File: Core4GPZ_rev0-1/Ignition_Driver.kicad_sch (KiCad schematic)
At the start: 10 parts, among them Q1 FGP3440G2-F085, Q2 FGP3440G2-F085

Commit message: Reworked the VR conditionner
Schematic and PCB based on the Dropbear model
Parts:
- renumbered D1 to D5, D2 to D6, R1 to R3, R3 to R5
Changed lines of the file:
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@@
 		(dnp no)
 		(fields_autoplaced yes)
-		(property "Reference" "R1"
+		(property "Reference" "R3"
 			(at 76.2 54.61 90)
 			(effects
@@
 			(project "Core4GPZ_rev0-1"
 				(path "/ac28f42d-34b3-4fcc-84dd-ab6106f99610/d5427090-fd08-4b35-ae6e-bc2a7b0d4087"
-					(reference "R1")
+					(reference "R3")
 					(unit 1)
 				)
@@
 		(dnp no)
 		(fields_autoplaced yes)
-		(property "Reference" "#PWR010"
+		(property "Reference" "#PWR08"
 			(at 90.17 85.09 0)
 			(effects
@@
 			(project "Core4GPZ_rev0-1"
 				(path "/ac28f42d-34b3-4fcc-84dd-ab6106f99610/d5427090-fd08-4b35-ae6e-bc2a7b0d4087"
-					(reference "#PWR010")
+					(reference "#PWR08")
 					(unit 1)
 				)
@@
 		(dnp no)
 		(fields_autoplaced yes)
-		(property "Reference" "D1"
+		(property "Reference" "D5"
 			(at 101.6 60.9599 90)
 			(effects
@@
 			(project "Core4GPZ_rev0-1"
 				(path "/ac28f42d-34b3-4fcc-84dd-ab6106f99610/d5427090-fd08-4b35-ae6e-bc2a7b0d4087"
-					(reference "D1")
+					(reference "D5")
 					(unit 1)
 				)
@@
 		(dnp no)
 		(fields_autoplaced yes)
-		(property "Reference" "D2"
+		(property "Reference" "D6"
 			(at 186.69 60.9599 90)
 			(effects
@@
 			(project "Core4GPZ_rev0-1"
 				(path "/ac28f42d-34b3-4fcc-84dd-ab6106f99610/d5427090-fd08-4b35-ae6e-bc2a7b0d4087"
-					(reference "D2")
+					(reference "D6")
 					(unit 1)
 				)
@@
 		(dnp no)
 		(fields_autoplaced yes)
-		(property "Reference" "R3"
+		(property "Reference" "R5"
 			(at 161.29 54.61 90)
 			(effects
@@
 			(project "Core4GPZ_rev0-1"
 				(path "/ac28f42d-34b3-4fcc-84dd-ab6106f99610/d5427090-fd08-4b35-ae6e-bc2a7b0d4087"
-					(reference "R3")
-					(unit 1)
-				)
+					(reference "R5")
+					(unit 1)
+				)

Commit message: Modified GND Plane. Reworked routing
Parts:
- renumbered R2 to R3, R3 to R4, R4 to R5, R5 to R6
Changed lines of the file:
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@@
 		(dnp no)
 		(fields_autoplaced yes)
-		(property "Reference" "R3"
+		(property "Reference" "R4"
 			(at 76.2 54.61 90)
 			(effects
@@
 			(project "Core4GPZ_rev0-1"
 				(path "/ac28f42d-34b3-4fcc-84dd-ab6106f99610/d5427090-fd08-4b35-ae6e-bc2a7b0d4087"
-					(reference "R3")
+					(reference "R4")
 					(unit 1)
 				)
@@
 		(dnp no)
 		(fields_autoplaced yes)
-		(property "Reference" "R4"
+		(property "Reference" "R5"
 			(at 157.48 67.3099 0)
 			(effects
@@
 			(project "Core4GPZ_rev0-1"
 				(path "/ac28f42d-34b3-4fcc-84dd-ab6106f99610/d5427090-fd08-4b35-ae6e-bc2a7b0d4087"
-					(reference "R4")
+					(reference "R5")
 					(unit 1)
 				)
@@
 		(dnp no)
 		(fields_autoplaced yes)
-		(property "Reference" "R2"
+		(property "Reference" "R3"
 			(at 72.39 66.0399 0)
 			(effects
@@
 			(project "Core4GPZ_rev0-1"
 				(path "/ac28f42d-34b3-4fcc-84dd-ab6106f99610/d5427090-fd08-4b35-ae6e-bc2a7b0d4087"
-					(reference "R2")
+					(reference "R3")
 					(unit 1)
 				)
@@
 		(dnp no)
 		(fields_autoplaced yes)
-		(property "Reference" "R5"
+		(property "Reference" "R6"
 			(at 161.29 54.61 90)
 			(effects
@@
 			(project "Core4GPZ_rev0-1"
 				(path "/ac28f42d-34b3-4fcc-84dd-ab6106f99610/d5427090-fd08-4b35-ae6e-bc2a7b0d4087"
-					(reference "R5")
-					(unit 1)
-				)
+					(reference "R6")
+					(unit 1)
+				)

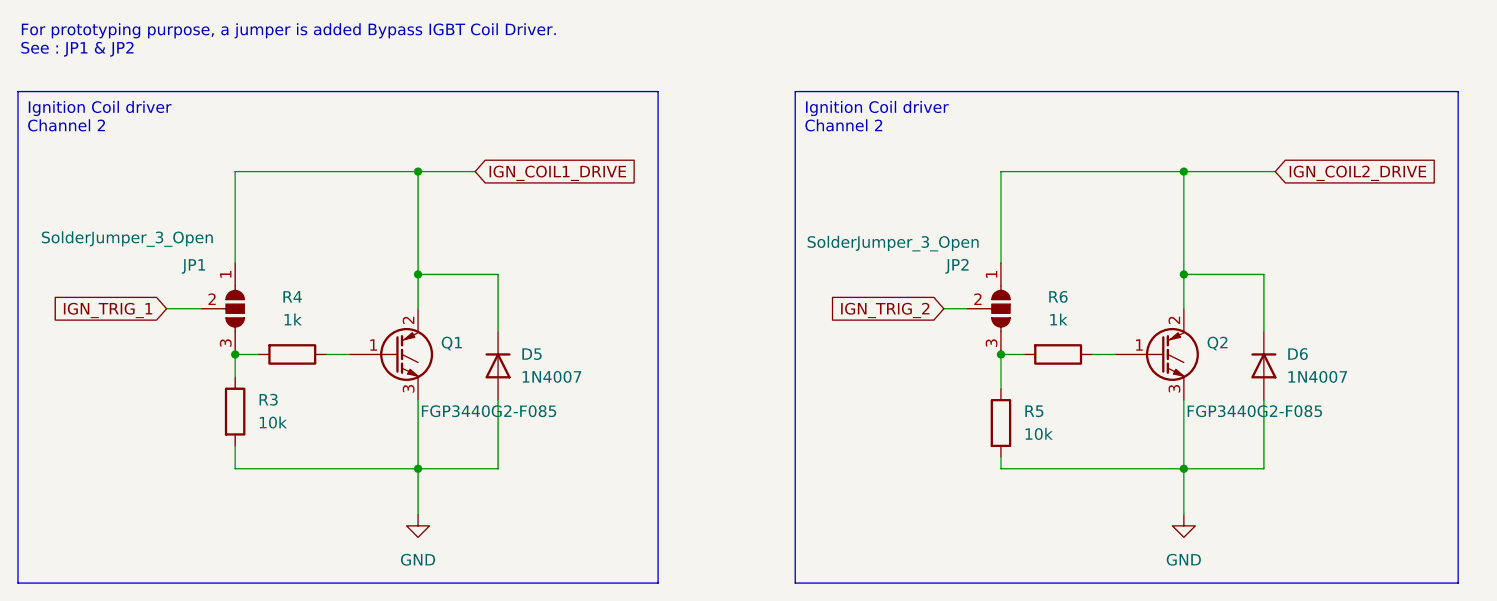
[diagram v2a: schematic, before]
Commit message: Implemented DRV8825 and upgrade IGN Driver
Ignition drivers upgraded with SMD IGBT FGD3440
Added Stepper Driver DRV8825
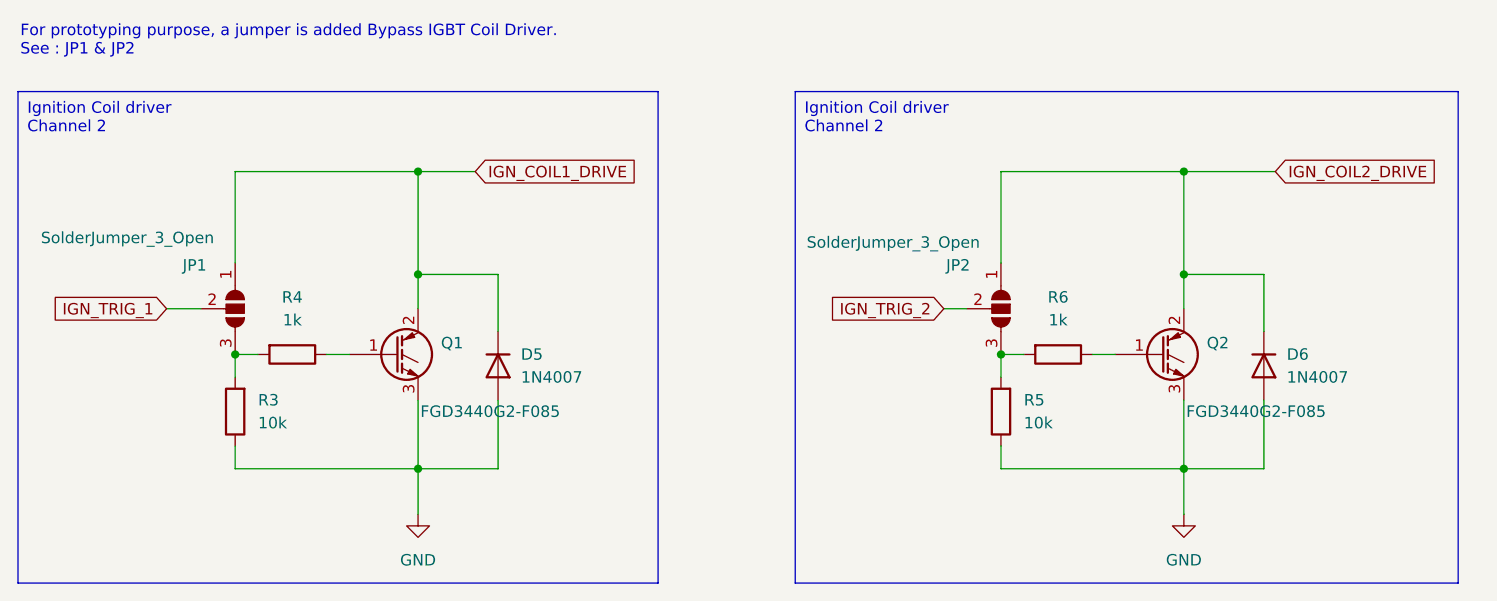
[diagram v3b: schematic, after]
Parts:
- Q1, Q2: value FGP3440G2-F085 -> FGD3440G2-F085; footprint Package_TO_SOT_THT:TO-220-3_Vertical -> Package_TO_SOT_SMD:TO-252-2
- R3, R4, R5, R6: footprint Resistor_THT:R_Axial_DIN0204_L3.6mm_D1.6mm_P5.08mm_Horizontal -> Resistor_SMD:R_0805_2012Metric
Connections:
- net GND: now also R3.1, R5.1; no longer R3.2, R5.2
- net at JP1.3 (B), R4.2: now also R3.2; no longer R3.1
- net at JP2.3 (B), R6.2: now also R5.2; no longer R5.1
